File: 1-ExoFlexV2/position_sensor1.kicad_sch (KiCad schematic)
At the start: 24 parts, among them J100 Jumper, J101 Jumper, J102 Jumper, U67 COMP, U68 COMP, U69 COMP, U70 AND Gate, U71 AND Gate, U72 Inverter

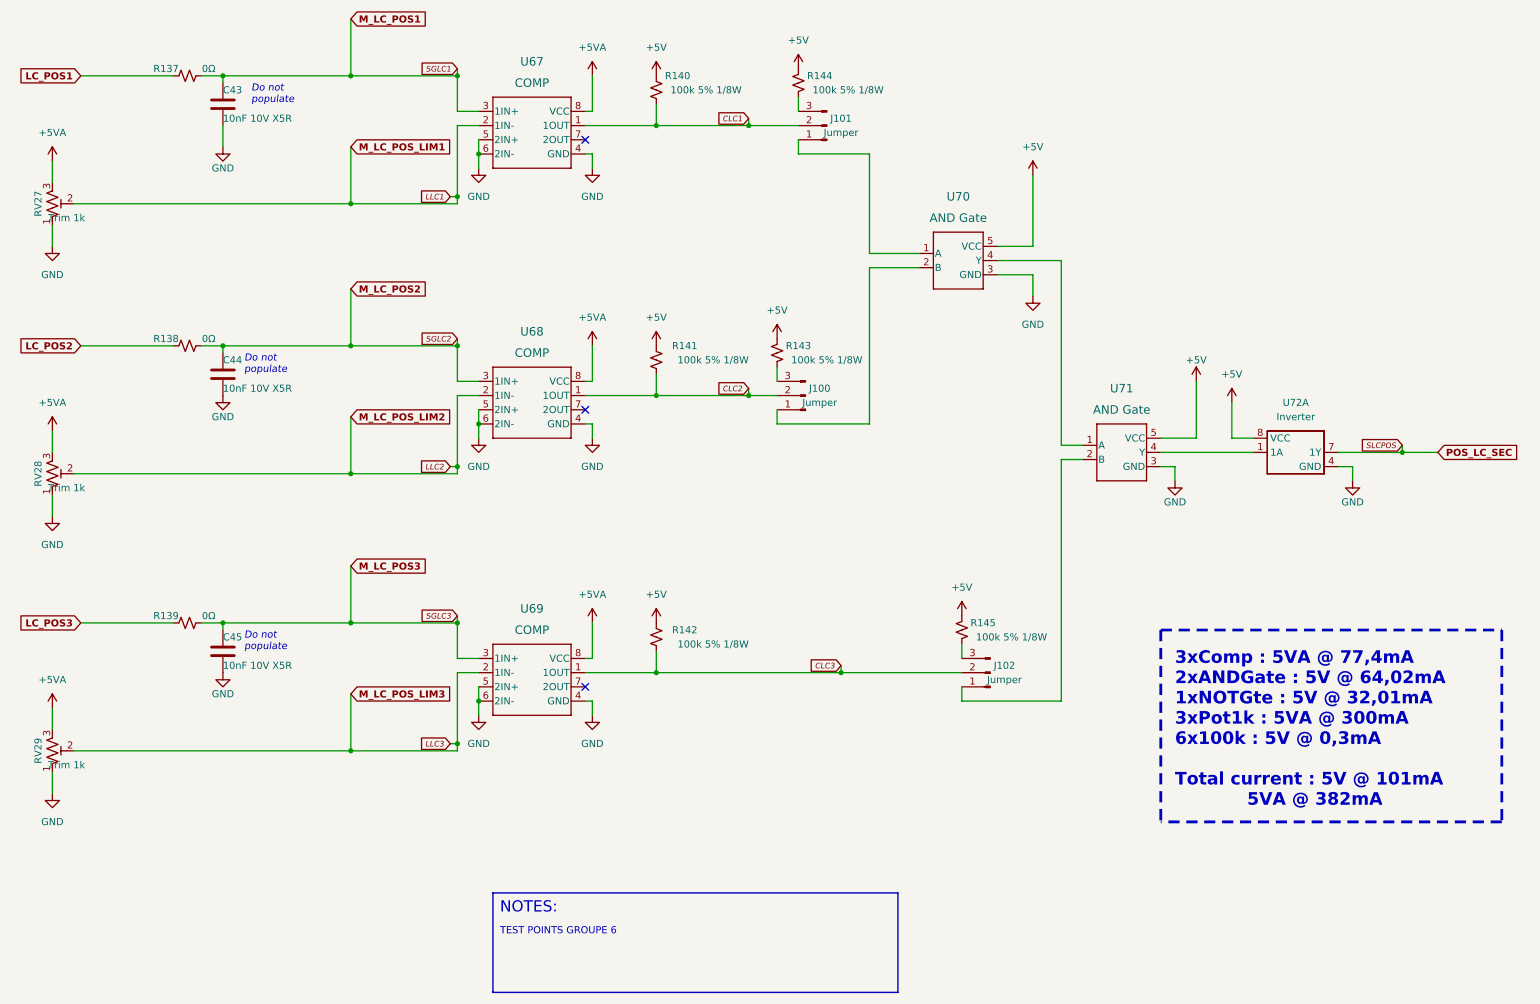
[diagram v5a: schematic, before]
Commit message: Finalisation 3
- Changement des régulateur de tension
- Retrait de test point inutile
- Changement de jumper mal positionner
- Ajout de Mounting holes et fiducial
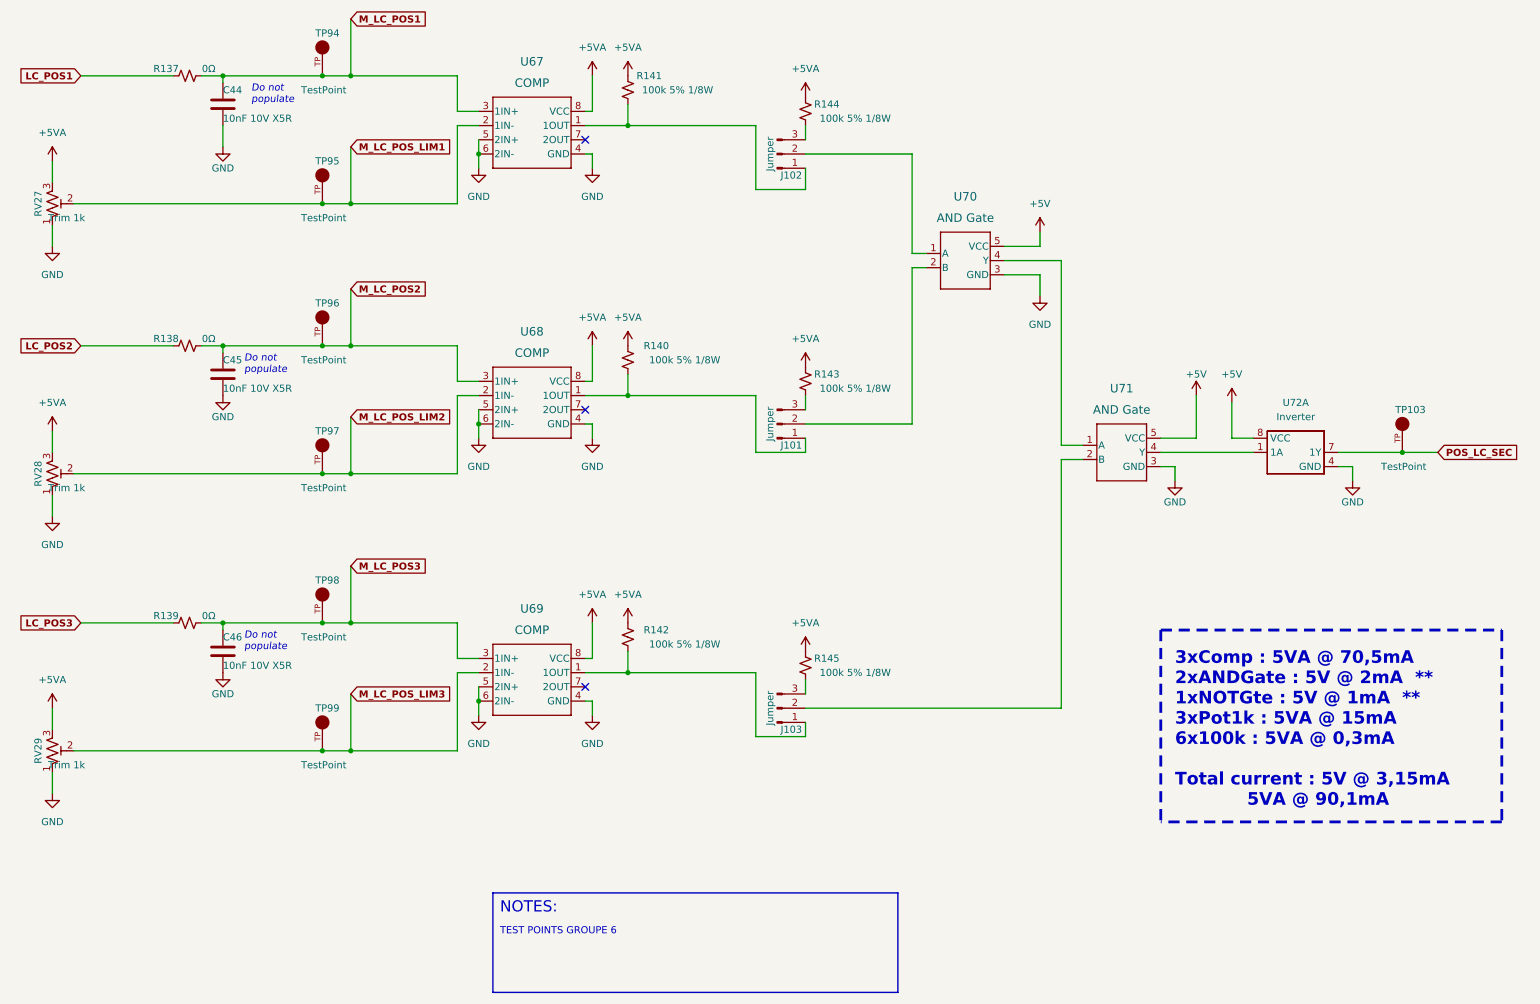
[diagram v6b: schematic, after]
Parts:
- removed C43: 10nF 10V X5R, Capacitor_SMD:C_01005_0402Metric, symbol Device:C
- added C46: 10nF 10V X5R, Capacitor_SMD:C_0603_1608Metric, symbol Device:C
- added TP103, TP94, TP95, TP96, TP97, TP98, TP99: TestPoint, FootPrint:KEYSTONE_5005, symbol SymLib:5005
- C44, C45: footprint Capacitor_SMD:C_01005_0402Metric -> Capacitor_SMD:C_0603_1608Metric; DESCRIPTION 10000 pF ±10% 10V Ceramic Capacitor X5R 01005 (0402 Metric) -> 10000 pF ±5% 10V Ceramic Capacitor U2J 0603 (1608 Metric); PACKAGE 01005 (0402 Metric) -> 0603 (1608 Metric); PART NUMBER GRM022R61A103KE19L -> GRM1857U1A103JA44D
- J101: renamed from J100; footprint Connector_PinSocket_2.54mm:PinSocket_1x03_P2.54mm_Vertical -> Connector_PinHeader_2.54mm:PinHeader_1x03_P2.54mm_Vertical
- J102: renamed from J101; footprint Connector_PinSocket_2.54mm:PinSocket_1x03_P2.54mm_Vertical -> Connector_PinHeader_2.54mm:PinHeader_1x03_P2.54mm_Vertical
- J103: renamed from J102; footprint Connector_PinSocket_2.54mm:PinSocket_1x03_P2.54mm_Vertical -> Connector_PinHeader_2.54mm:PinHeader_1x03_P2.54mm_Vertical
- renumbered R141 to R140, R140 to R141
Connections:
- net +5V: no longer R140.1, R141.1, R142.1, R143.2, R144.2, R145.2
- net +5VA: now also R140.1, R141.1, R142.1, R143.2, R144.2, R145.2
- net GND: now also C46.2
- net M_LC_POS1: now also C44.1, TP94.TP
- net M_LC_POS2: now also C45.1, TP96.TP; no longer C44.1
- net M_LC_POS3: now also C46.1, TP98.TP; no longer C45.1
- net POS_LC_SEC: now also TP103.TP
- net at U71.2 (B): now also J103.2 (Pin_2); no longer J103.1 (Pin_1)
- net at J102.1 (Pin_1): now also R141.2, U67.1 (1OUT); no longer U70.1 (A)
- net at J101.1 (Pin_1): now also R140.2, U68.1 (1OUT); no longer U70.2 (B)
- removed net CLC1: J102.2 (Pin_2), R141.2, U67.1 (1OUT)
- removed net CLC2: J101.2 (Pin_2), R140.2, U68.1 (1OUT)
- net CLC3: no longer names the net of R142.2, U69.1 (1OUT)
- net CLC3: now also J103.1 (Pin_1); no longer J103.2 (Pin_2)
- net LLC1 renamed M_LC_POS_LIM1
- net M_LC_POS_LIM1: now also TP95.TP
- net LLC2 renamed M_LC_POS_LIM2
- net M_LC_POS_LIM2: now also TP97.TP
- net LLC3 renamed M_LC_POS_LIM3
- net M_LC_POS_LIM3: now also TP99.TP
- new net: J102.2 (Pin_2), U70.1 (A)
- new net: J101.2 (Pin_2), U70.2 (B)
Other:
- note added: "3xComp : 5VA @ 70,5mA 2xANDGate : 5V @ 2mA ** 1xNOTGte : 5V @ 1mA ** 3xPot1k : 5VA @ 15mA 6x100k : 5VA @ 0,3mA Total current : 5V @ 3,15mA 5VA @ 90,1mA"
- note removed: "3xComp : 5VA @ 77,4mA 2xANDGate : 5V @ 64,02mA 1xNOTGte : 5V @ 32,01mA 3xPot1k : 5VA @ 300mA 6x100k : 5V @ 0,3mA Total current : 5V @ 101mA 5VA @ 382mA"
- moved on the sheet: J101, J102, J103, R140, R141, R142, R143, R144, R145, U70

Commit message: Finalisation schéma FIN
- Changement des uméro pour les inverseurs
- Changement des connecteur et début de placement
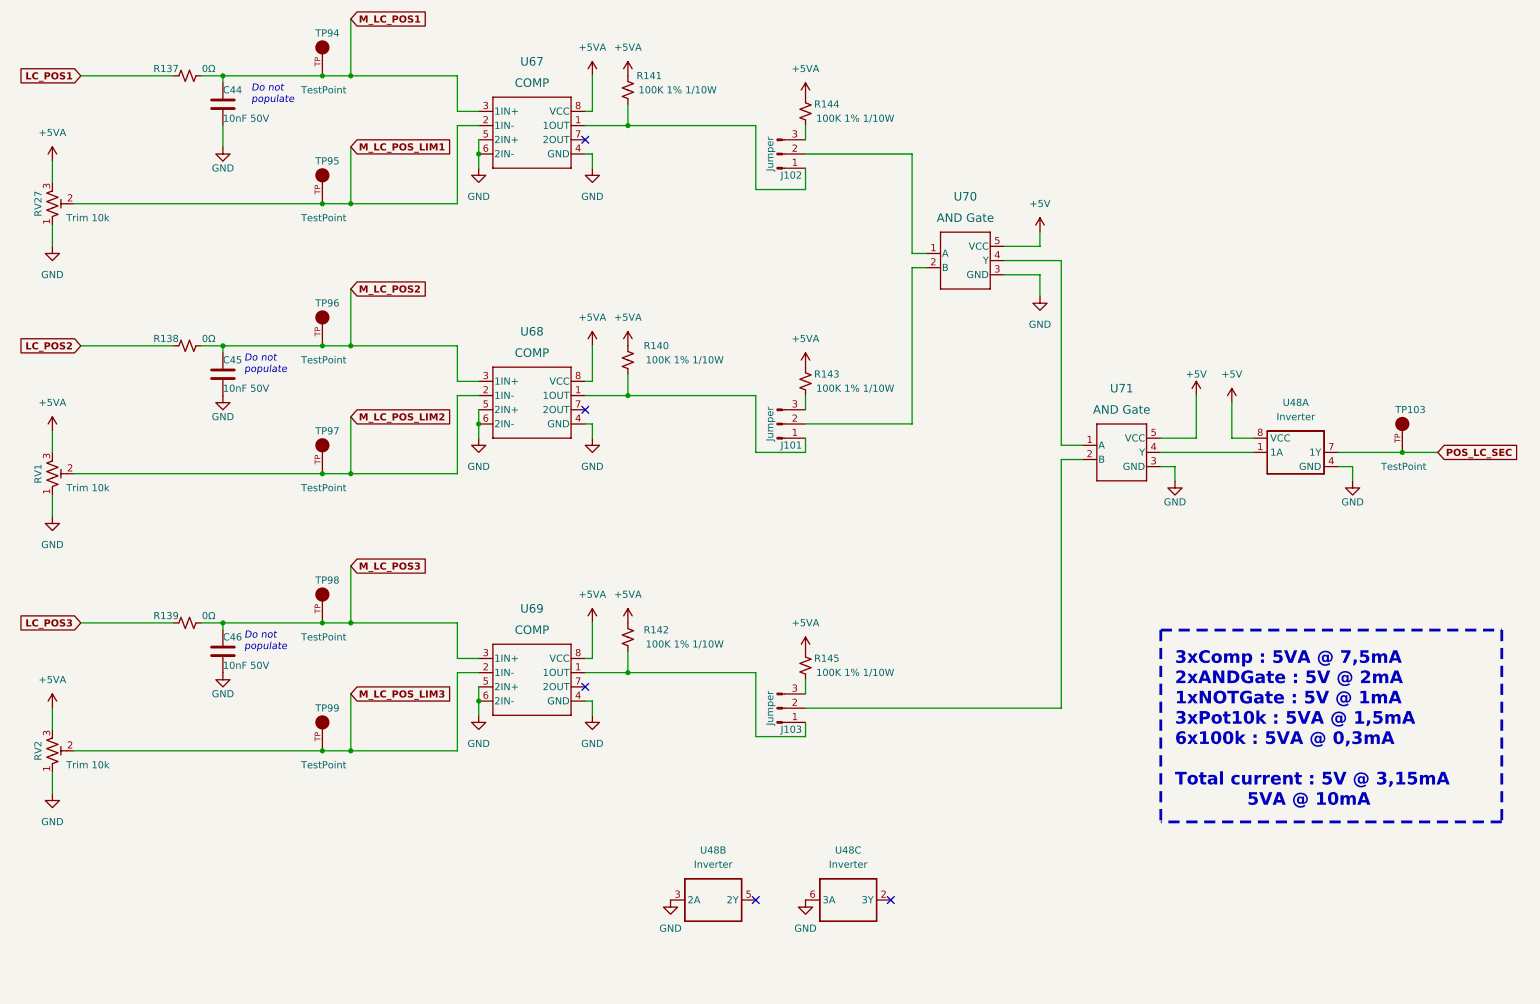
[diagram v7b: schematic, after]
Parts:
- removed RV28, RV29: Trim 1k, FootPrint:TRIM_3362P-1-102LF, symbol Device:R_Potentiometer_Trim_US
- removed U72: Inverter, FootPrint:SN74LVC3G14DCUT, symbol SymLib:SN74LVC3G14DCUT_V2
- added RV1, RV2: Trim 10k, FootPrint:TRIM_3362P-1-103LF, symbol Device:R_Potentiometer_Trim_US
- added U48: Inverter, FootPrint:SN74LVC3G14DCUT, symbol SymLib:SN74LVC3G14DCUT_V2
- C44, C45, C46: value 10nF 10V X5R -> 10nF 50V; footprint Capacitor_SMD:C_0603_1608Metric -> Capacitor_SMD:C_0805_2012Metric; DESCRIPTION 10000 pF ±5% 10V Ceramic Capacitor U2J 0603 (1608 Metric) -> 10000 pF ±5% 50V Ceramic Capacitor C0G, NP0 0805 (2012 Metr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; PACKAGE 0603 (1608 Metric) -> 0805 (2012 Metric); PART NUMBER GRM1857U1A103JA44D -> GRM2195C1H103JA01D
- R140, R141, R142, R143, R144, R145: value 100k 5% 1/8W -> 100K 1% 1/10W; footprint Resistor_SMD:R_0805_2012Metric -> Resistor_SMD:R_0603_1608Metric; DESCRIPTION 100 kOhms ±5% 0.125W, 1/8W Chip Resistor 0805 (2012 Metric)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 -> 100 kOhms ±1% 0.1W, 1/10W Chip Resistor 0603 (1608 Metric) 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; PACKAGE 0805 (2012 Metric) -> 0603 (1608 Metric); PART NUMBER ERJ-6GEYJ104V -> ERJ-3EKF1003V
- RV27: value Trim 1k -> Trim 10k; footprint FootPrint:TRIM_3362P-1-102LF -> FootPrint:TRIM_3362P-1-103LF; DESCRIPTION Trimmer 1k 0,5W PC PIN TOP -> 10 kOhms 0.5W, 1/2W PC Pins Through Hole Trimmer Potentiome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; PART NUMBER 3362P-1-102LF -> 3362P-1-103LF
- TP103, TP94, TP95, TP96, TP97, TP98, TP99: NOTES (none) -> DO NOT POPULATE; PURCHASE-URL https://pricing.snapeda.com/search/part/5005/?ref=eda -> (none)
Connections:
- net +5V: now also U48.8 (VCC)
- net +5VA: now also RV1.3, RV2.3
- net GND: now also RV1.1, RV2.1, U48.3 (2A), U48.4 (GND), U48.6 (3A)
- net M_LC_POS_LIM2: now also RV1.2
- net M_LC_POS_LIM3: now also RV2.2
- net POS_LC_SEC: now also U48.7 (1Y)
- net at U71.4 (Y): now also U48.1 (1A)
- no-connect marks 3 -> 5
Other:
- note added: "3xComp : 5VA @ 7,5mA 2xANDGate : 5V @ 2mA 1xNOTGate : 5V @ 1mA 3xPot10k : 5VA @ 1,5mA 6x100k : 5VA @ 0,3mA Total current : 5V @ 3,15mA 5VA @ 10mA"
- note removed: "3xComp : 5VA @ 70,5mA 2xANDGate : 5V @ 2mA ** 1xNOTGte : 5V @ 1mA ** 3xPot1k : 5VA @ 15mA 6x100k : 5VA @ 0,3mA Total current : 5V @ 3,15mA 5VA @ 90,1mA"
- note removed: "NOTES:"
- note removed: "TEST POINTS GROUPE 6"

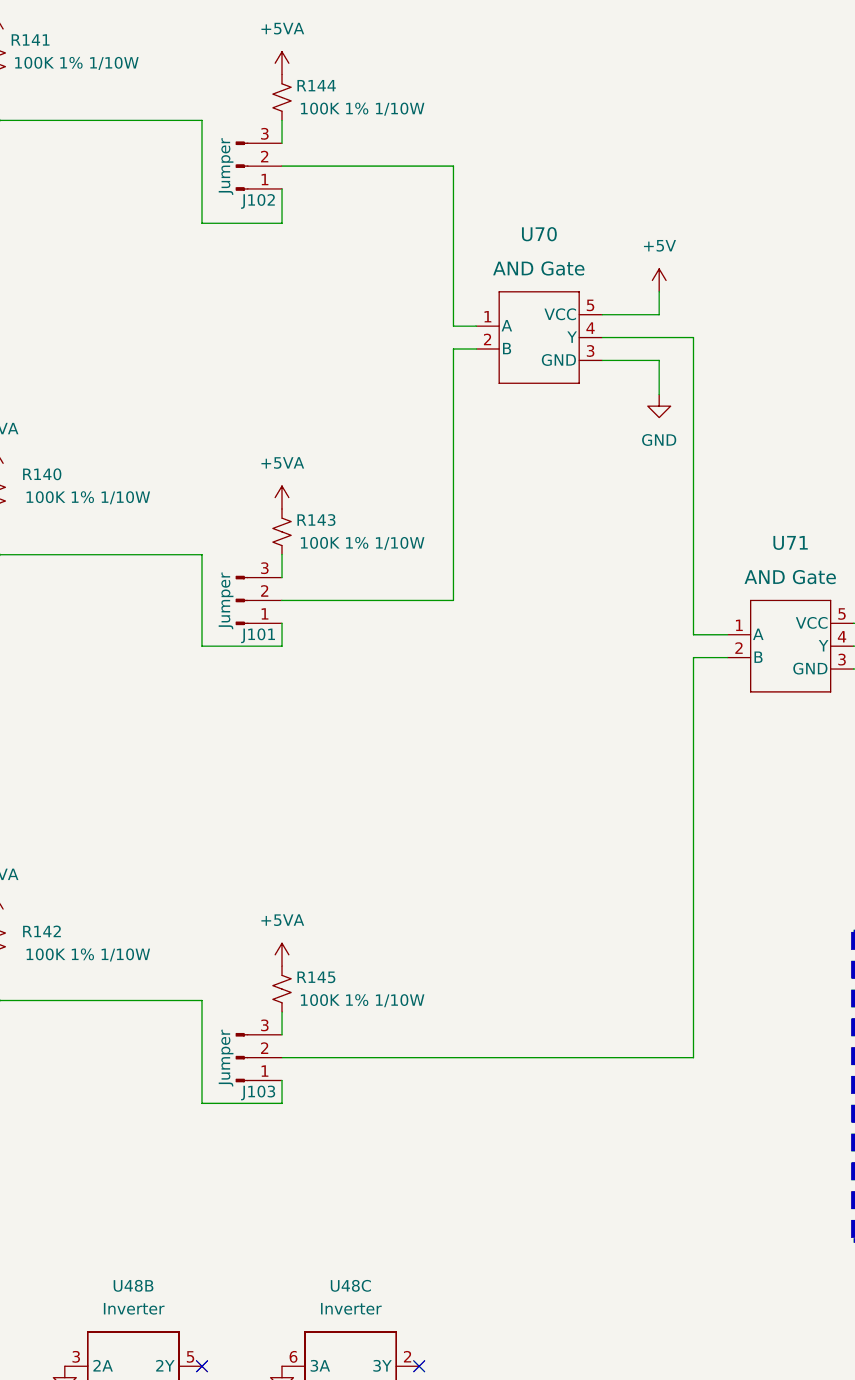
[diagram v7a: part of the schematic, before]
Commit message: Routage pour Review 1
- Replacement des test point pour faciliter le rework
- Correction des erreurs dans le BOM
-
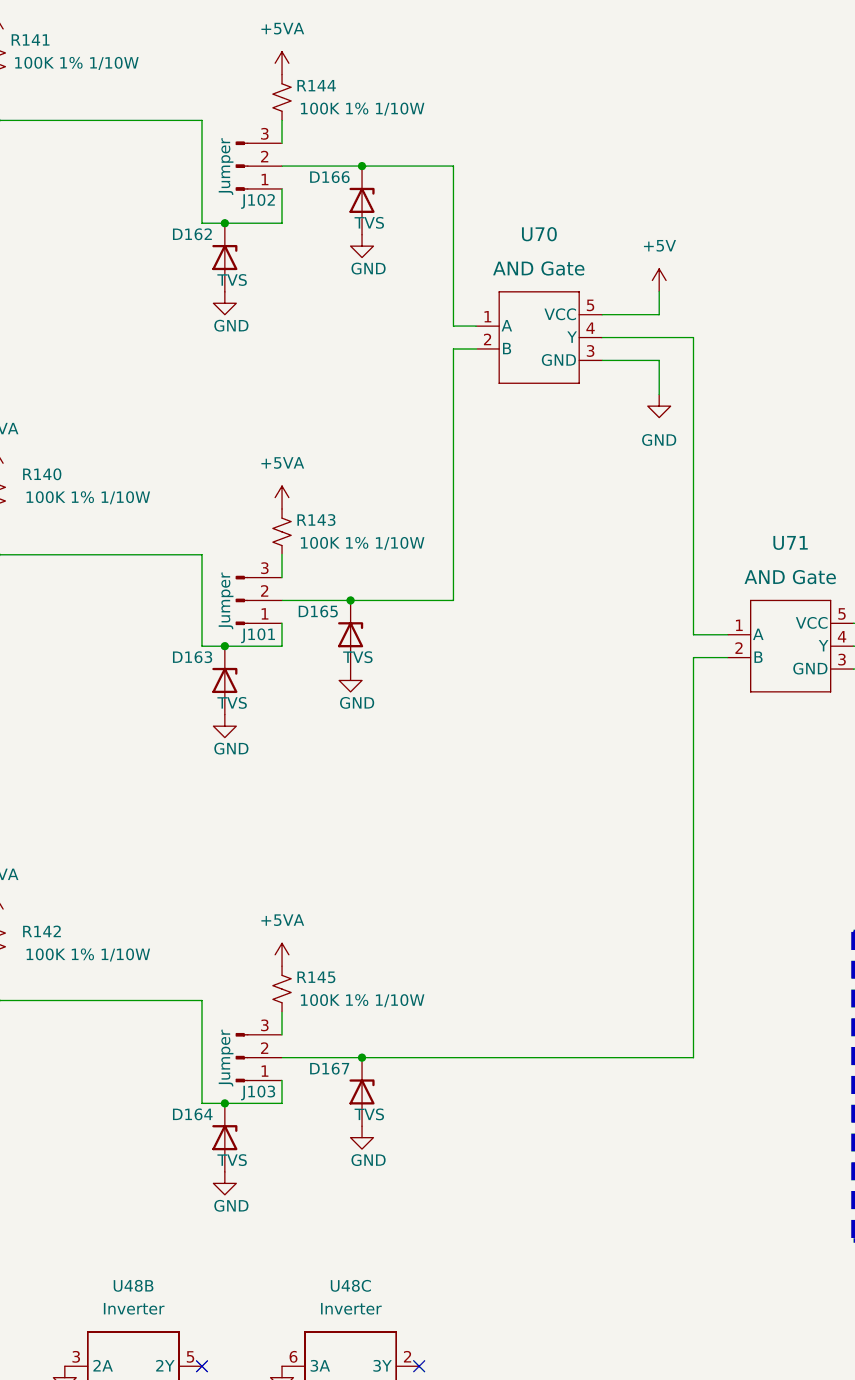
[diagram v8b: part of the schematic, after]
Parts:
- added D162, D163, D164, D165, D166, D167: TVS, FootPrint:DPY2_TEX, symbol Device:D_Zener
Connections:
- net GND: now also D162.2 (A), D163.2 (A), D164.2 (A), D165.2 (A), D166.2 (A), D167.2 (A)
- net at J102.1 (Pin_1), R141.2, U67.1 (1OUT): now also D162.1 (K)
- net at J103.2 (Pin_2), U71.2 (B): now also D167.1 (K)
- net at J103.1 (Pin_1), R142.2, U69.1 (1OUT): now also D164.1 (K)
- net at J101.1 (Pin_1), R140.2, U68.1 (1OUT): now also D163.1 (K)
- net at J102.2 (Pin_2), U70.1 (A): now also D166.1 (K)
- net at J101.2 (Pin_2), U70.2 (B): now also D165.1 (K)
